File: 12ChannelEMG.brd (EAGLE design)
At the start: 47.4 x 269.2 mm, 243 parts

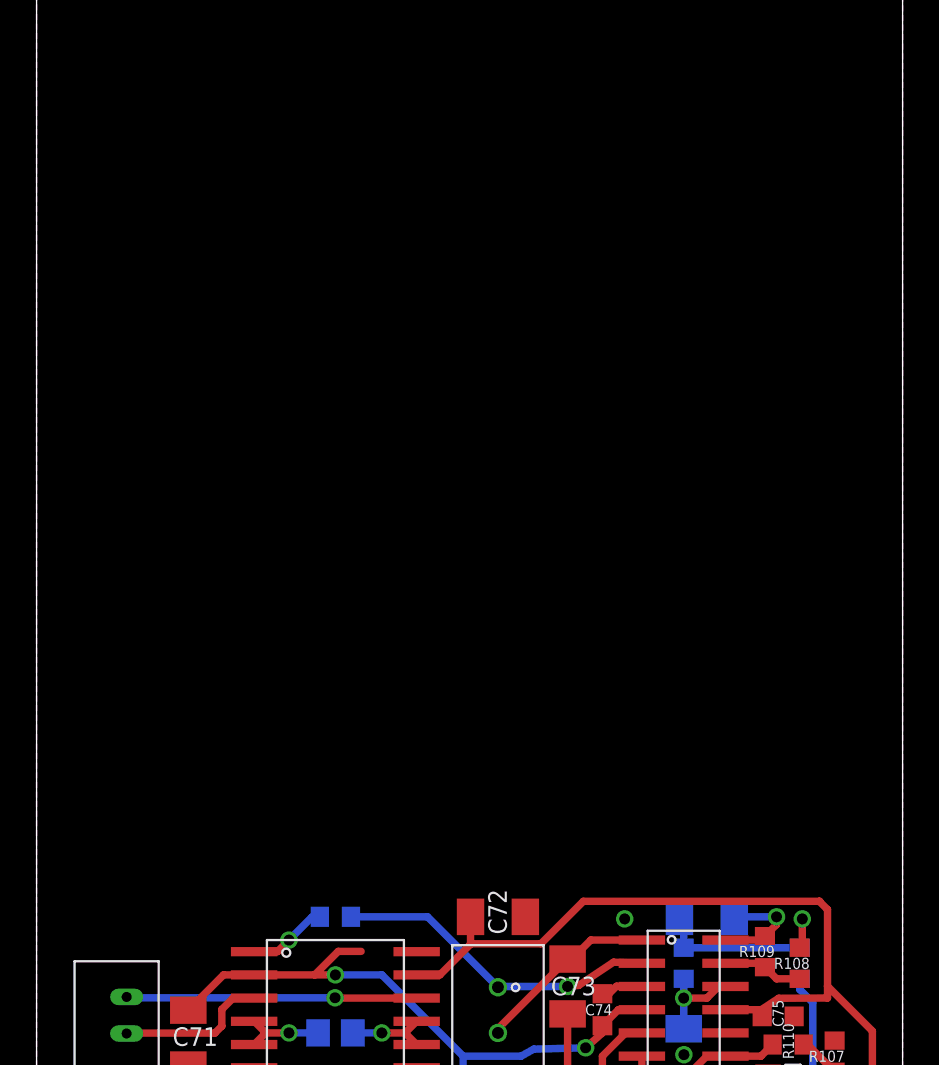
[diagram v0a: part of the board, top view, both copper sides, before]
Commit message: Channel 14, all channels done
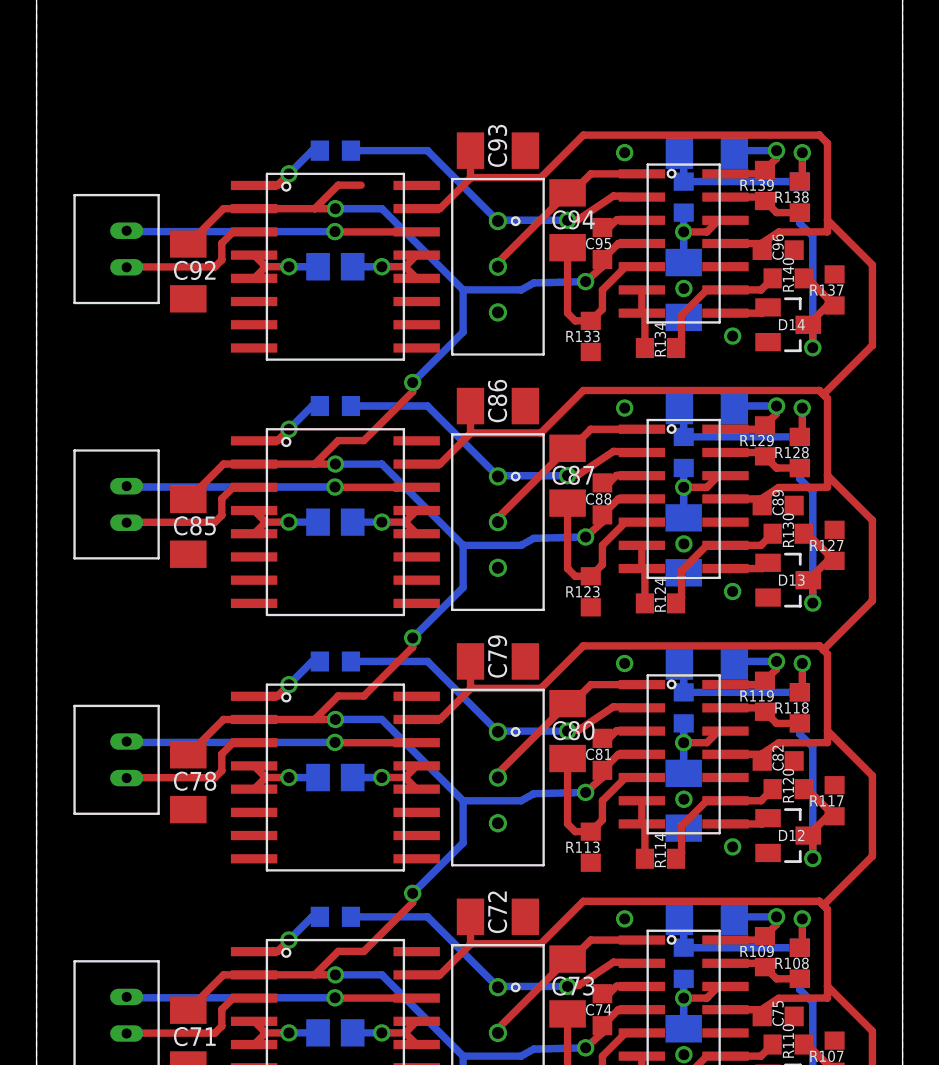
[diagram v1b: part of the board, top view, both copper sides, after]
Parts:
- added C78, C79, C83, C84, C85, C86, C90, C91, C92, C93, C97, C98: 0.1uF, resistor:C1206K
- added C80, C87, C94: 3.3uF, resistor:C1206K
- added C81, C82, C88, C89, C95, C96: 0.22uF, rcl:C0603K
- added D12, D13, D14: BAT54, diode:SOT23
- added R111, R121, R131: 50k, rcl:R0805
- added R112, R120, R122, R130, R132, R140: 100, resistor:R0603
- added R113, R123, R133: 10k, rcl:R0603
- added R114, R124, R134: 200, rcl:R0603
- added R115, R116, R125, R126, R135, R136: 82k, resistor:R0603
- added R117, R127, R137: 300, resistor:R0603
- added R118, R128, R138: 100k, resistor:R0603
- added R119, R129, R139: 56k, resistor:R0603
- added U$45, U$49, U$53: INA101KU, 12-ChannelEMG:SOIC167.5MM
- added U$46, U$50, U$54: LMC6492, 12-ChannelEMG:SOIC14
- added U$47, U$51, U$55: PV36504, 12-ChannelEMG:PV36W
- added U$48, U$52, U$56: 2PIN, 12-ChannelEMG:2PIN
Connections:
- new net N$179: R111.2, U$45.12, U$45.13
- new net N$180: U$45.3, U$48.2
- new net N$181: R112.2, U$46.2, U$47.1
- new net N$182: R112.1, U$45.1
- new net N$183: C80.1, U$46.1, U$47.2
- new net N$184: C80.2, R113.2, U$46.5
- new net N$185: R114.1, U$46.6, U$46.7
- new net N$186: R114.2, R120.1, U$46.9
- new net N$187: D12.1, U$46.8
- new net N$188: C83.1, R116.1, U$46.12
- new net N$189: D12.3, R115.1, R117.1, R120.2
- new net N$190: C84.2, R119.2, U$46.14
- new net N$191: R118.1, R119.1, U$46.13
- new net N$192: C84.1, R115.2, R116.2
- new net N$193: R111.1, U$45.4, U$45.5
- new net N$194: U$45.14, U$48.1
- new net N$195: R121.2, U$49.12, U$49.13
- new net N$196: U$49.3, U$52.2
- new net N$197: R122.2, U$50.2, U$51.1
- new net N$198: R122.1, U$49.1
- new net N$199: C87.1, U$50.1, U$51.2
- new net N$200: C87.2, R123.2, U$50.5
- new net N$201: R124.1, U$50.6, U$50.7
- new net N$202: R124.2, R130.1, U$50.9
- new net N$203: D13.1, U$50.8
- new net N$204: C90.1, R126.1, U$50.12
- new net N$205: D13.3, R125.1, R127.1, R130.2
- new net N$206: C91.2, R129.2, U$50.14
- new net N$207: R128.1, R129.1, U$50.13
- new net N$208: C91.1, R125.2, R126.2
- new net N$209: R121.1, U$49.4, U$49.5
- new net N$210: U$49.14, U$52.1
- new net N$211: R131.2, U$53.12, U$53.13
- new net N$212: U$53.3, U$56.2
- new net N$213: R132.2, U$54.2, U$55.1
- new net N$214: R132.1, U$53.1
- new net N$215: C94.1, U$54.1, U$55.2
- new net N$216: C94.2, R133.2, U$54.5
- new net N$217: R134.1, U$54.6, U$54.7
- new net N$218: R134.2, R140.1, U$54.9
- new net N$219: D14.1, U$54.8
- new net N$220: C97.1, R136.1, U$54.12
- new net N$221: D14.3, R135.1, R137.1, R140.2
- new net N$222: C98.2, R139.2, U$54.14
- new net N$223: R138.1, R139.1, U$54.13
- new net N$224: C98.1, R135.2, R136.2
- new net N$225: R131.1, U$53.4, U$53.5
- new net N$226: U$53.14, U$56.1
- net GND: now also C78.2, C79.2, C81.2, C82.2, C83.2, C85.2, C86.2, C88.2, C89.2, C90.2, C92.2, C93.2, C95.2, C96.2, C97.2, R113.1, R117.2, R118.2, R123.1, R127.2, R128.2, R133.1, R137.2, R138.2, U$46.10, U$46.3, U$50.10, U$50.3, U$54.10, U$54.3
- net VCC+: now also C78.1, C81.1, C85.1, C88.1, C92.1, C95.1, U$45.2, U$46.4, U$49.2, U$50.4, U$53.2, U$54.4
- net VCC-: now also C79.1, C82.1, C86.1, C89.1, C93.1, C96.1, U$45.15, U$46.11, U$49.15, U$50.11, U$53.15, U$54.11
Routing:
- net VCC-: track 522.5 -> 668.2 mm
- net VCC+: track 455.0 -> 582.0 mm, vias 32 -> 41
- net N$213: track 0.00 -> 18.0 mm, vias 0 -> 1
- net N$197: track 0.00 -> 18.0 mm, vias 0 -> 1
- net N$181: track 0.00 -> 18.0 mm, vias 0 -> 1
- net N$226: track 0.00 -> 15.9 mm, vias 0 -> 1
- net N$210: track 0.00 -> 15.9 mm, vias 0 -> 1
- net N$194: track 0.00 -> 15.9 mm, vias 0 -> 1
- net N$221: track 0.00 -> 13.4 mm, vias 0 -> 1
- net N$205: track 0.00 -> 13.4 mm, vias 0 -> 1
- net N$189: track 0.00 -> 13.4 mm, vias 0 -> 1
- net GND: track 44.6 -> 56.7 mm, vias 44 -> 56
- net N$215: track 0.00 -> 10.1 mm
- net N$199: track 0.00 -> 10.1 mm
- net N$183: track 0.00 -> 10.1 mm
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
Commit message: Added power connector
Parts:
- added U$57: 3PIN, 12-ChannelEMG:3PIN
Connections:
- net GND: now also U$57.1
- net VCC+: now also U$57.3
- net VCC-: now also U$57.2
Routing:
- net VCC+: track 582.0 -> 610.0 mm
- net VCC-: track 668.2 -> 673.5 mm
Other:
- board size 47.4 x 269.2 mm -> 57.5 x 196.8 mm
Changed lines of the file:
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@@
 <board>
 <plain>
-<wire x1="0" y1="0" x2="47.371" y2="0" width="0" layer="20"/>
-<wire x1="47.371" y1="0" x2="47.371" y2="269.24" width="0" layer="20"/>
-<wire x1="47.371" y1="269.24" x2="0" y2="269.24" width="0" layer="20"/>
-<wire x1="0" y1="269.24" x2="0" y2="0" width="0" layer="20"/>
+<wire x1="0" y1="0" x2="57.531" y2="0" width="0" layer="20"/>
+<wire x1="57.531" y1="0" x2="57.531" y2="196.85" width="0" layer="20"/>
+<wire x1="57.531" y1="196.85" x2="0" y2="196.85" width="0" layer="20"/>
+<wire x1="0" y1="196.85" x2="0" y2="0" width="0" layer="20"/>
 </plain>
 <attributes>
@@
 </element>
 <element name="U$56" library="12-ChannelEMG" package="2PIN" value="2PIN" x="4.9276" y="189.1665"/>
+<element name="U$57" library="12-ChannelEMG" package="3PIN" value="3PIN" x="47.244" y="5.08" rot="R180"/>
 </elements>
 <signals>
@@
 <via x="20.574" y="181.864" extent="1-16" drill="0.6"/>
 <wire x1="17.907" y1="178.689" x2="20.574" y2="181.356" width="0.4064" layer="1"/>
+<contactref element="U$57" pad="3"/>
+<wire x1="47.244" y1="7.08" x2="46.704" y2="7.08" width="0.4064" layer="16"/>
+<wire x1="46.704" y1="7.08" x2="45.212" y2="5.588" width="0.4064" layer="16"/>
+<wire x1="45.212" y1="5.588" x2="45.212" y2="3.048" width="0.4064" layer="16"/>
+<wire x1="45.212" y1="3.048" x2="42.926" y2="0.762" width="0.4064" layer="16"/>
+<wire x1="42.926" y1="0.762" x2="29.21" y2="0.762" width="0.4064" layer="16"/>
+<wire x1="29.21" y1="0.762" x2="26.924" y2="3.048" width="0.4064" layer="16"/>
+<wire x1="26.924" y1="3.048" x2="26.924" y2="5.278596875" width="0.4064" layer="16"/>
+<wire x1="26.924" y1="5.278596875" x2="27.220109375" y2="5.57470625" width="0.4064" layer="16"/>
 </signal>
 <signal name="N$2">
@@
 <wire x1="45.72" y1="183.896" x2="45.719996875" y2="183.896" width="0.4064" layer="1"/>
 <wire x1="45.719996875" y1="183.896" x2="43.03359375" y2="181.209596875" width="0.4064" layer="1"/>
+<contactref element="U$57" pad="2"/>
+<wire x1="47.244" y1="5.08" x2="46.58010625" y2="5.08" width="0.4064" layer="1"/>
+<wire x1="46.58010625" y1="5.08" x2="43.289565625" y2="8.370540625" width="0.4064" layer="1"/>
 </signal>
 <signal name="GND">
@@
 <polygon width="0.4064" layer="1">
 <vertex x="0" y="0"/>
-<vertex x="47.371" y="0"/>
-<vertex x="47.371" y="269.24"/>
-<vertex x="0" y="269.24"/>
+<vertex x="57.531" y="0"/>
+<vertex x="57.531" y="196.85"/>
+<vertex x="0" y="196.85"/>
 </polygon>
 <polygon width="0.4064" layer="16">
 <vertex x="0" y="0"/>
-<vertex x="47.371" y="0"/>
-<vertex x="47.371" y="269.24"/>
-<vertex x="0" y="269.24"/>
+<vertex x="57.531" y="0"/>
+<vertex x="57.531" y="196.85"/>
+<vertex x="0" y="196.85"/>
 </polygon>
 <via x="32.1945" y="12.7" extent="1-16" drill="0.6"/>
@@
 <wire x1="31.7246" y1="190.754" x2="33.095084375" y2="190.754" width="0.4064" layer="1"/>
 <wire x1="33.095084375" y1="190.754" x2="33.1107375" y2="190.738346875" width="0.4064" layer="1"/>
+<contactref element="U$57" pad="1"/>
 </signal>
 <signal name="N$6">
@@
 </signal>
 </signals>
+<errors>
+</errors>
 </board>
 </drawing>

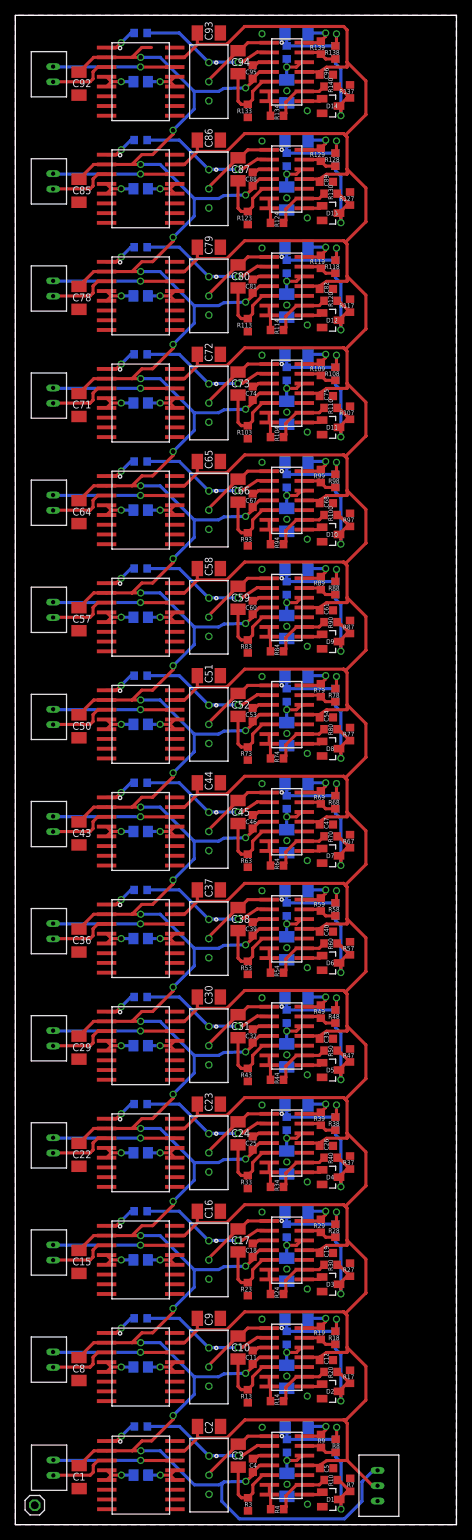
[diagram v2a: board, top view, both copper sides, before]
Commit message: Added 15 pin output
Board finished, need to add silk screen markings
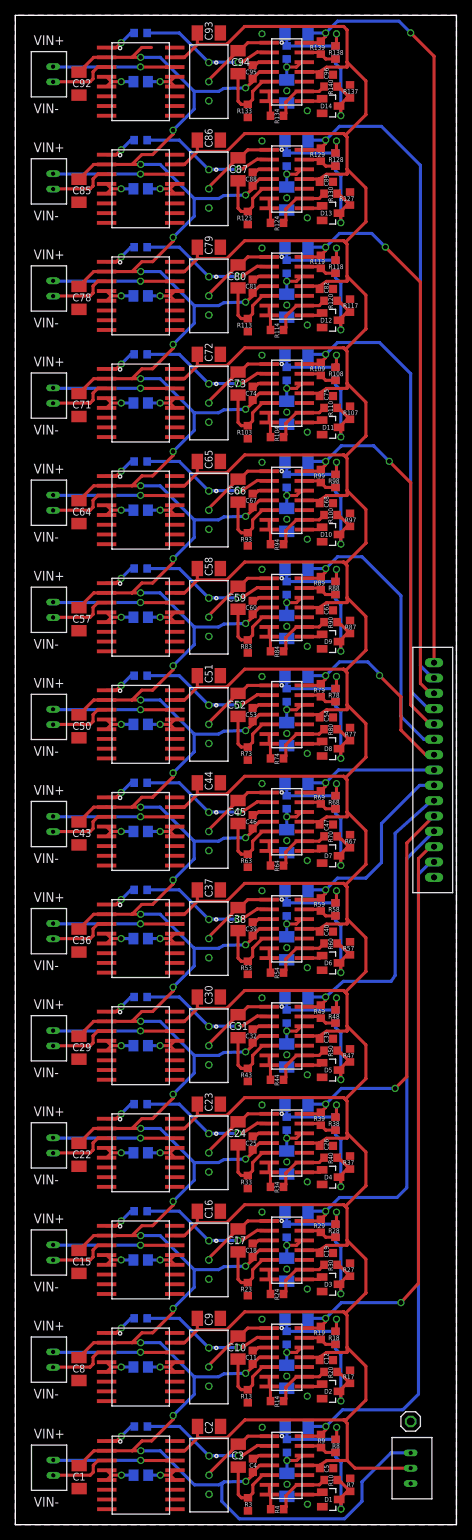
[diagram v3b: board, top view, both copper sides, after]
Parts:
- added U$58: 15PIN, 12-ChannelEMG:15PIN
- moved GND 50.2 mm to (51.6, 13.5)
- moved U$57 4.89 mm to (51.6, 7.37)
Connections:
- net GND: now also U$58.15
- net N$110: now also U$58.8
- net N$126: now also U$58.7
- net N$14: now also U$58.14
- net N$142: now also U$58.6
- net N$158: now also U$58.5
- net N$174: now also U$58.4
- net N$190: now also U$58.3
- net N$206: now also U$58.2
- net N$222: now also U$58.1
- net N$30: now also U$58.13
- net N$46: now also U$58.12
- net N$62: now also U$58.11
- net N$78: now also U$58.10
- net N$94: now also U$58.9
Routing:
- net N$222: track 5.88 -> 101.7 mm, vias 1 -> 2
- net N$14: track 5.88 -> 90.4 mm
- net N$206: track 5.88 -> 88.8 mm
- net N$30: track 5.88 -> 78.0 mm, vias 1 -> 2
- net N$190: track 5.88 -> 76.3 mm, vias 1 -> 2
- net N$46: track 5.88 -> 65.7 mm
- net N$174: track 5.88 -> 64.7 mm
- net N$62: track 5.88 -> 53.5 mm, vias 1 -> 2
- net N$158: track 5.88 -> 52.9 mm, vias 1 -> 2
- net N$78: track 5.88 -> 41.4 mm
- net N$142: track 5.88 -> 39.8 mm
- net N$94: track 5.88 -> 28.6 mm
- net N$126: track 5.88 -> 28.5 mm, vias 1 -> 2
- net N$110: track 5.88 -> 20.7 mm
- net VCC+: track 610.0 -> 615.3 mm
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
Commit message: Shrank board, added silk screening
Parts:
- moved U$58 2.74 mm to (51.9, 98.4)
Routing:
- net N$110: track 20.7 -> 18.0 mm
- net N$30: track 78.0 -> 76.1 mm
- net N$14: track 90.4 -> 88.5 mm
- net N$62: track 53.5 -> 51.7 mm
- net N$46: track 65.7 -> 64.1 mm
- net N$78: track 41.4 -> 40.0 mm
- net N$206: track 88.8 -> 87.7 mm
- net N$158: track 52.9 -> 51.9 mm
- net N$174: track 64.7 -> 63.8 mm
- net N$222: track 101.7 -> 100.9 mm
- net N$94: track 28.6 -> 28.0 mm
- net N$126: track 28.5 -> 28.0 mm
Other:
- board size 57.5 x 196.8 mm -> 54.6 x 196.8 mm
- board text added: "Electrode"
- board text added: "GND"
- board text added: "IN1"
- board text added: "IN10"
- board text added: "IN11"
- board text added: "IN12"
- board text added: "IN13"
- board text added: "IN14"
- board text added: "IN2"
- board text added: "IN3"
- board text added: "IN4"
- board text added: "IN5"
- board text added: "IN6"
- board text added: "IN7"
- board text added: "IN8"
- board text added: "IN9"
- board text added: "OUT1"
- board text added: "OUT10"
- board text added: "OUT11"
- board text added: "OUT12"
- board text added: "OUT13"
- board text added: "OUT14"
- board text added: "OUT2"
- board text added: "OUT3"
- board text added: "OUT4"
- board text added: "OUT5"
- board text added: "OUT6"
- board text added: "OUT7"
- board text added: "OUT8"
- board text added: "OUT9"
- board text added: "VCC+"
- board text added: "VCC-"
